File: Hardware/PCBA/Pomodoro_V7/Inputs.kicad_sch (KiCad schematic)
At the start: 2 parts, among them J1 Conn_01x02_Socket

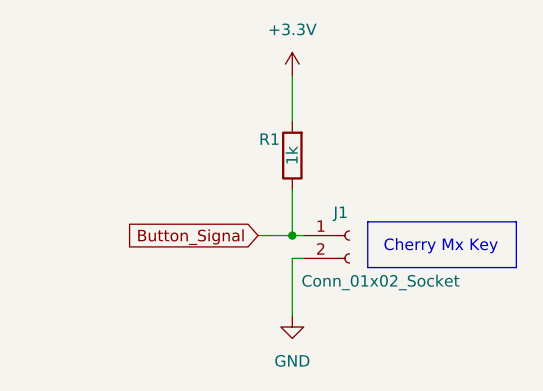
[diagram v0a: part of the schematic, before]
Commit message: Verified the microcontroller Pinout; Added basic peripheral wiring; Added the USBC Wiring
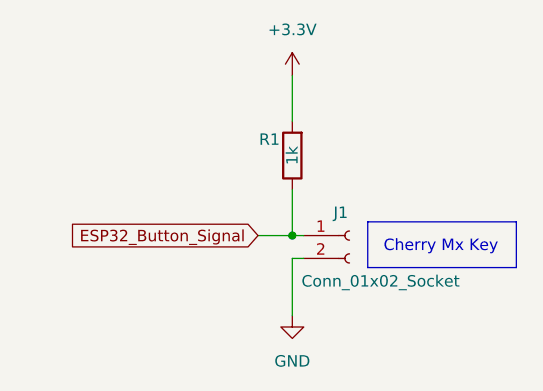
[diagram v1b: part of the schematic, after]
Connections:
- net Button_Signal renamed ESP32_Button_Signal
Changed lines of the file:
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@@
 		)
 	)
-	(global_label "Button_Signal"
+	(global_label "ESP32_Button_Signal"
 		(shape input)
 		(at 49.53 54.61 180)
@@
 		)
 		(property "Intersheetrefs" "${INTERSHEET_REFS}"
-			(at 33.4823 54.61 0)
+			(at 26.4672 54.61 0)
 			(effects
 				(font

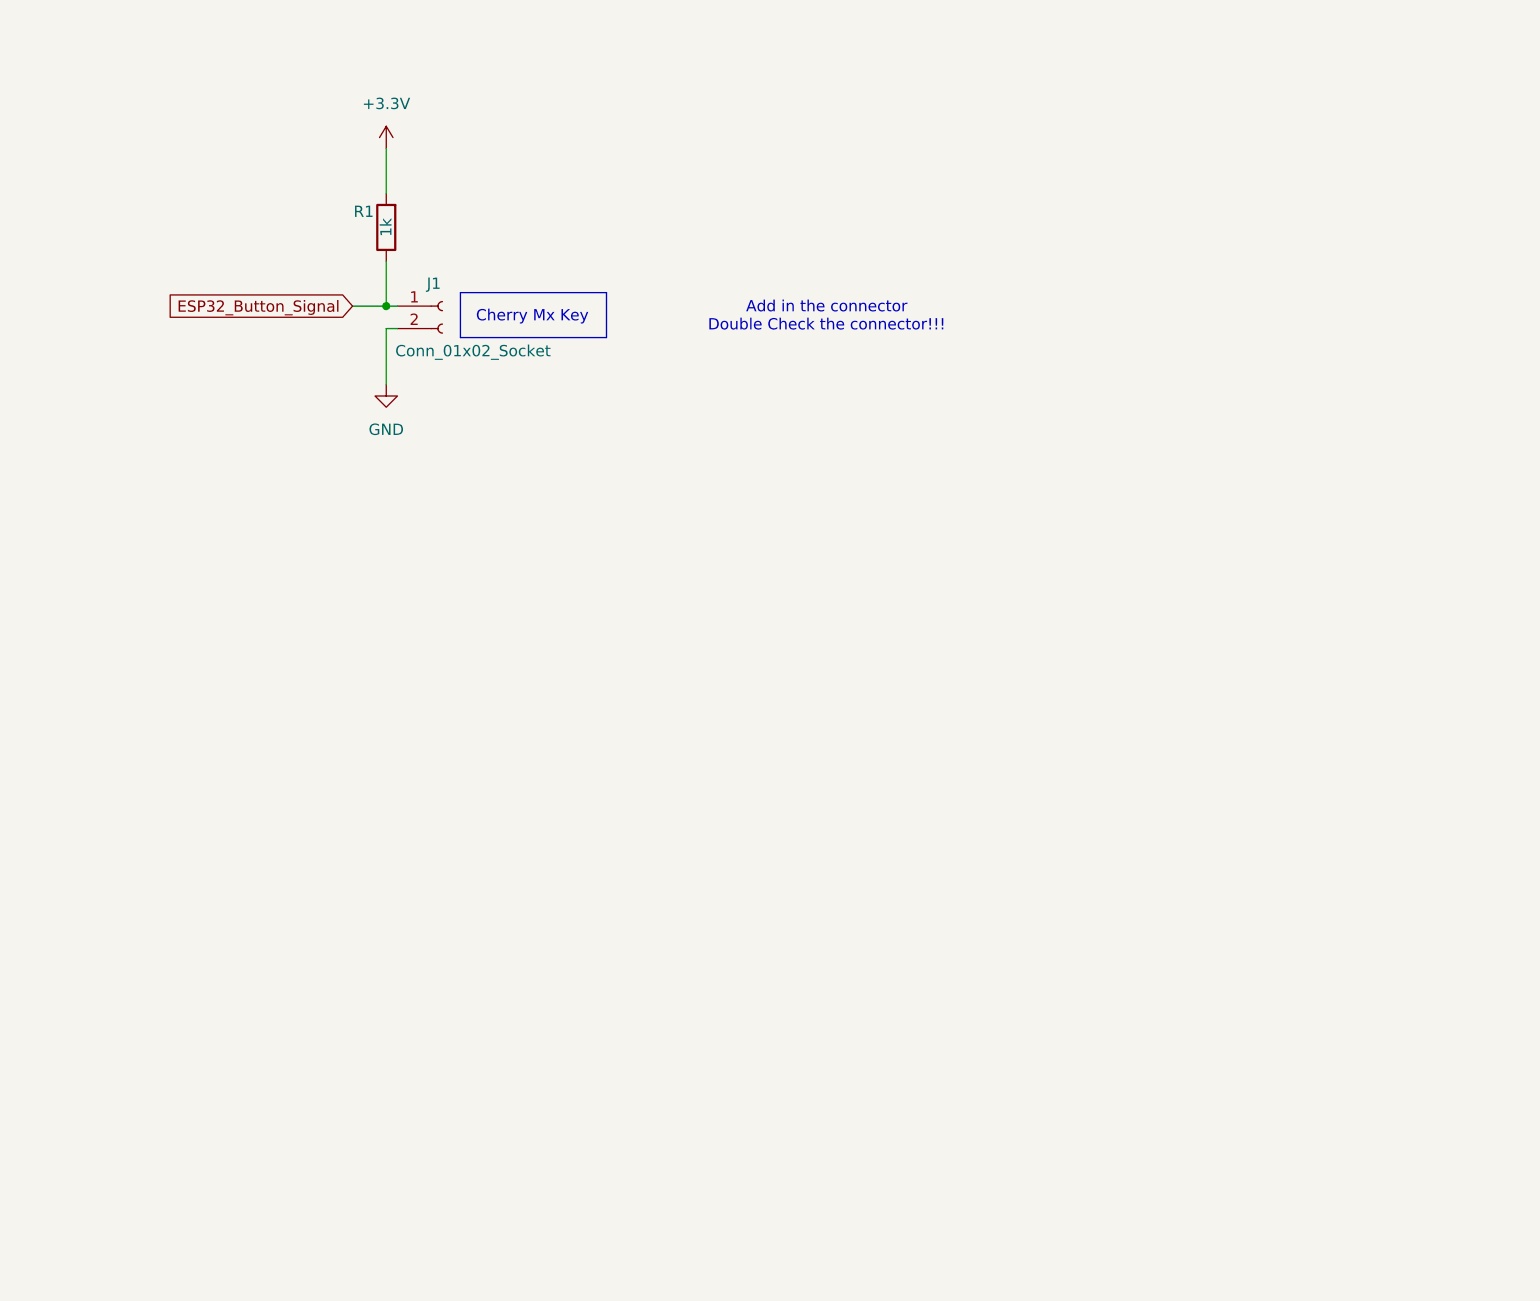
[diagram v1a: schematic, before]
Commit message: FW can now be flashed to an ESP32-S2 Target; Completed the Schematic
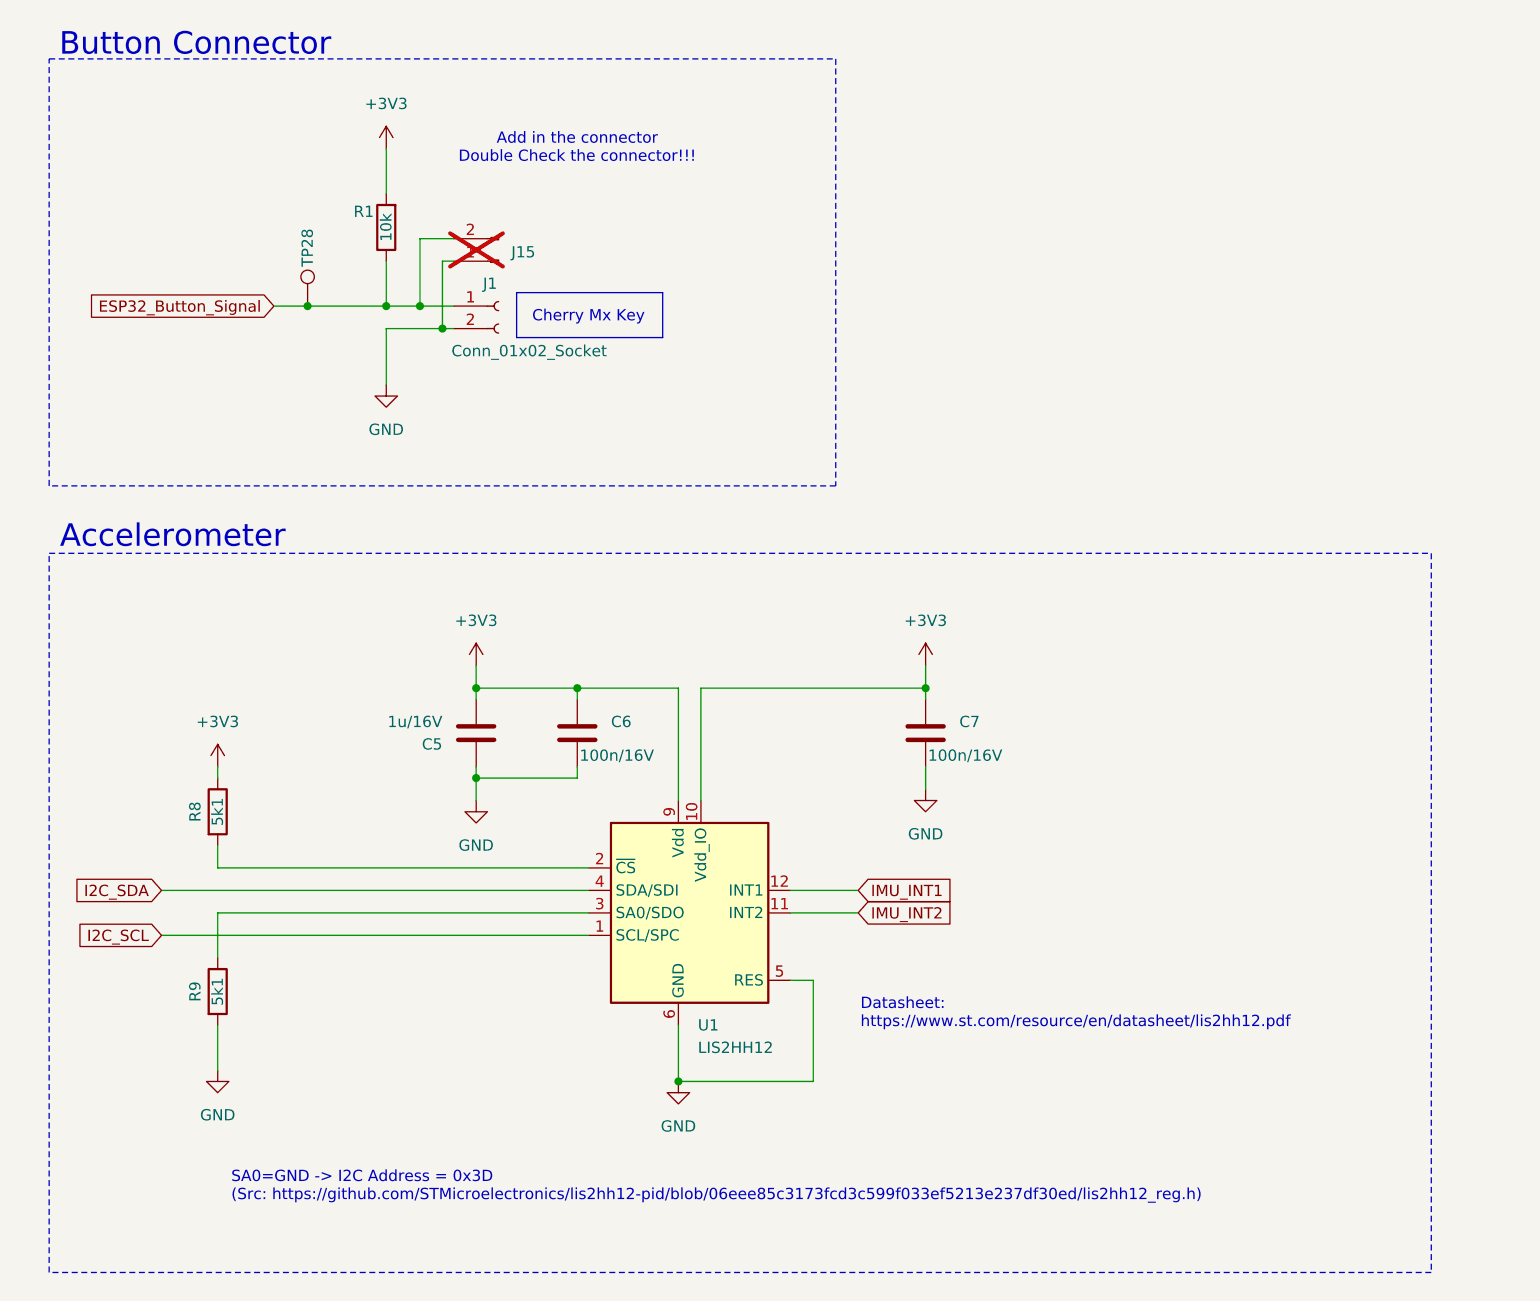
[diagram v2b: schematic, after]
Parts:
- added C5: 1u/16V, Capacitor_SMD:C_0805_2012Metric, symbol Device:C
- added C6, C7: 100n/16V, Capacitor_SMD:C_0805_2012Metric, symbol Device:C
- added J15: Conn_01x02_Pin, Connector_PinHeader_2.54mm:PinHeader_1x02_P2.54mm_Vertical, symbol Connector:Conn_01x02_Pin
- added R8, R9: 5k1, Resistor_SMD:R_0805_2012Metric, symbol Device:R
- added TP28: TestPoint, TestPoint:TestPoint_Pad_D1.0mm, symbol Connector:TestPoint
- added U1: LIS2HH12, Package_LGA:LGA-12_2x2mm_P0.5mm, symbol Sensor_Motion:LIS2HH12
- R1: value 1k -> 10k
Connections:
- net ESP32_Button_Signal: now also J15.2 (Pin_2), TP28.1
- net GND: now also C5.1, C6.1, C7.1, J15.1 (Pin_1), R9.2, U1.5 (RES), U1.6 (GND), U1.7 (GND), U1.8 (GND)
- net +3.3V renamed +3V3
- net +3V3: now also C5.2, C6.2, C7.2, R8.1, U1.10 (Vdd_IO), U1.9 (Vdd)
- new net: R8.2, U1.2 (~{CS})
- new net: R9.1, U1.3 (SA0/SDO)
- new net I2C_SCL: U1.1 (SCL/SPC)
- new net I2C_SDA: U1.4 (SDA/SDI)
- new net IMU_INT1: U1.12 (INT1)
- new net IMU_INT2: U1.11 (INT2)
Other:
- note added: "Accelerometer"
- note added: "Button Connector"
- note added: "Datasheet: https://www.st.com/resource/en/datasheet/lis2hh12.pdf"
- note added: "SA0=GND -> I2C Address = 0x3D (Src: https://github.com/STMicroelectronics/lis2hh12-pid/blob/06eee85c3173fcd3c599f033ef5213e237df30ed/lis2hh12_reg.h)"
- moved on the sheet: J1

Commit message: added the selector wheel, changed the Connectors on the Trigger Button to move the assemlby closer together
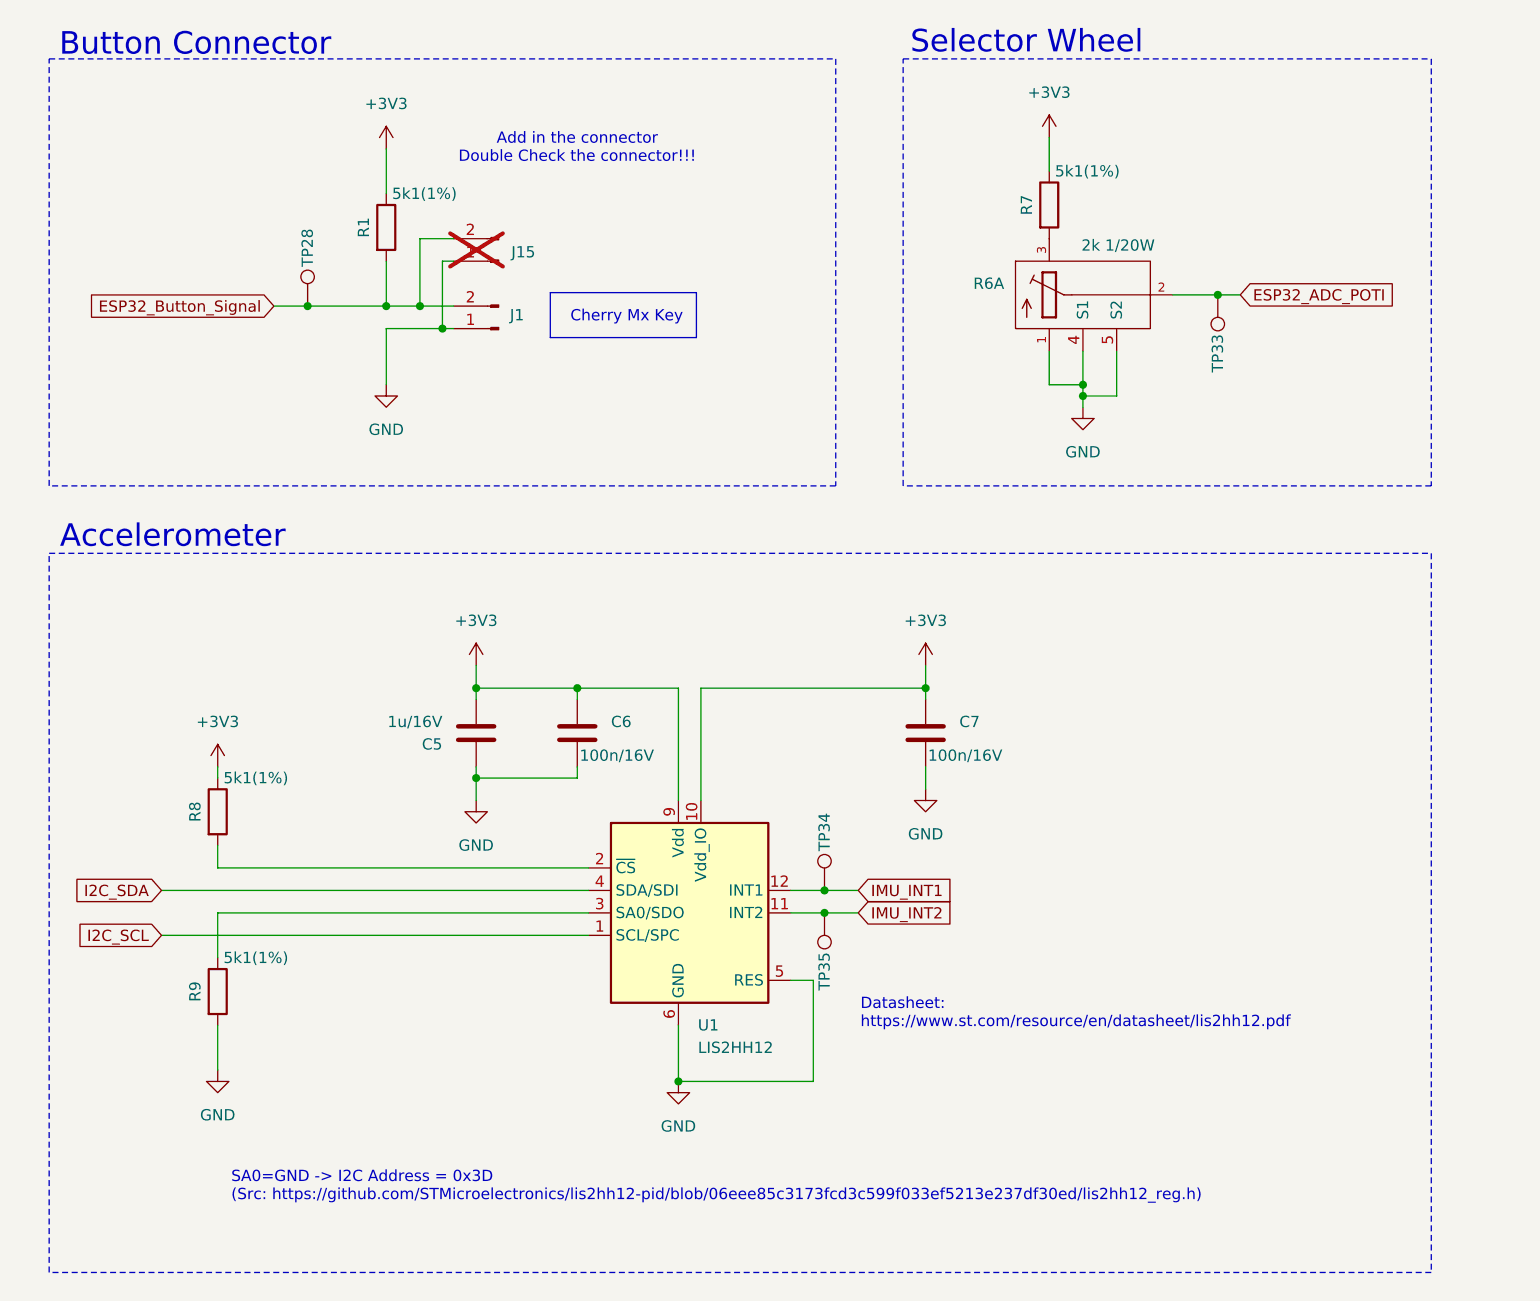
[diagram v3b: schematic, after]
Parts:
- removed J1: Conn_01x02_Socket, Connector_PinSocket_2.54mm:PinSocket_1x02_P2.54mm_Vertical_SMD_Pin1Right, symbol Connector:Conn_01x02_Socket
- added J1: Conn_01x02_Pin, Connector_PinHeader_2.54mm:PinHeader_1x02_P2.54mm_Horizontal, symbol Connector:Conn_01x02_Pin
- added R6: 2k 1/20W, Potentiometer_THT:Pot, symbol PTV09A-4025F-B103:PTV09A-4025F-B103
- added R7: 5k1(1%), Resistor_SMD:R_0805_2012Metric, symbol Device:R
- added TP33, TP34, TP35: TestPoint, TestPoint:TestPoint_Pad_D1.0mm, symbol Connector:TestPoint
- R1: value 10k -> 5k1(1%); MPN RC0805FR-07100RL -> CR0805-FX-5101ELF; Part ID (none) -> CR0805-FX-5101ELF
- R8, R9: value 5k1 -> 5k1(1%)
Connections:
- net +3V3: now also R1.1, R7.1; no longer R1.2
- net ESP32_Button_Signal: now also R1.2, J1.2 (Pin_2); no longer R1.1
- net GND: now also J1.1 (Pin_1), R6.1, R6.4 (S1), R6.5 (S2)
- net IMU_INT1: now also TP34.1
- net IMU_INT2: now also TP35.1
- new net: R6.3, R7.2
- new net ESP32_ADC_POTI: R6.2, TP33.1
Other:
- note added: "Selector Wheel"

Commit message: Update on the PCBA
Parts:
- R6: value 2k 1/20W -> 10k 1/20W; symbol PTV09A-4025F-B103:PTV09A-4025F-B103 -> Device:PTV09A-4025F-B103
- renumbered J1 to J10, J15 to J9, R7 to R4, R1 to R5, R8 to R7, R9 to R8, TP33 to TP22, TP28 to TP23, TP34 to TP24, TP35 to TP25
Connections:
- net GND: now also R6.3; no longer R6.1
- net at R4.2: now also R6.1; no longer R6.3
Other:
- moved on the sheet: R4, TP22

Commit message: Completed the PCBA Design - the formal part
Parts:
- removed J9: Conn_01x02_Pin, Connector_PinHeader_2.54mm:PinHeader_1x02_P2.54mm_Vertical, symbol Connector:Conn_01x02_Pin
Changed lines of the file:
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@@
-	)
-	(junction
-		(at 59.69 57.15)
-		(diameter 0)
-		(color 0 0 0 0)
 	)
 	(junction
@@
 	)
 	(junction
-		(at 57.15 54.61)
-		(diameter 0)
-		(color 0 0 0 0)
-	)
-	(junction
 		(at 63.5 97.79)
 		(diameter 0)
@@
 	(wire
 		(pts
-			(xy 57.15 46.99) (xy 57.15 54.61)
-		)
-		(stroke
-			(width 0)
-			(type default)
-		)
-	)
-	(wire
-		(pts
 			(xy 40.64 54.61) (xy 44.45 54.61)
 		)
@@
 	(wire
 		(pts
-			(xy 53.34 57.15) (xy 59.69 57.15)
+			(xy 53.34 57.15) (xy 60.96 57.15)
 		)
 		(stroke
@@
 	(wire
 		(pts
-			(xy 57.15 54.61) (xy 60.96 54.61)
+			(xy 53.34 54.61) (xy 60.96 54.61)
 		)
 		(stroke
@@
 	(wire
 		(pts
-			(xy 60.96 46.99) (xy 57.15 46.99)
-		)
-		(stroke
-			(width 0)
-			(type default)
-		)
-	)
-	(wire
-		(pts
-			(xy 59.69 49.53) (xy 59.69 57.15)
-		)
-		(stroke
-			(width 0)
-			(type default)
-		)
-	)
-	(wire
-		(pts
 			(xy 86.36 135.89) (xy 86.36 142.24)
 		)
@@
 	(wire
 		(pts
-			(xy 53.34 54.61) (xy 57.15 54.61)
-		)
-		(stroke
-			(width 0)
-			(type default)
-		)
-	)
-	(wire
-		(pts
 			(xy 146.05 33.02) (xy 146.05 35.56)
 		)
@@
 	(wire
 		(pts
-			(xy 60.96 49.53) (xy 59.69 49.53)
-		)
-		(stroke
-			(width 0)
-			(type default)
-		)
-	)
-	(wire
-		(pts
 			(xy 63.5 97.79) (xy 74.93 97.79)
 		)
@@
 		(pts
 			(xy 53.34 63.5) (xy 53.34 57.15)
-		)
-		(stroke
-			(width 0)
-			(type default)
-		)
-	)
-	(wire
-		(pts
-			(xy 59.69 57.15) (xy 60.96 57.15)
 		)
 		(stroke
@@
 	)
 	(symbol
-		(lib_id "Connector:Conn_01x02_Pin")
-		(at 66.04 49.53 180)
-		(unit 1)
-		(exclude_from_sim no)
-		(in_bom no)
-		(on_board yes)
-		(dnp yes)
-		(property "Reference" "J9"
-			(at 68.834 48.514 0)
-			(effects
-				(font
-					(size 1.27 1.27)
-				)
-			)
-		)
-		(property "Value" "Conn_01x02_Pin"
-			(at 65.405 52.07 0)
-			(effects
-				(font
-					(size 1.27 1.27)
-				)
-				(hide yes)
-			)
-		)
-		(property "Footprint" "Connector_PinHeader_2.54mm:PinHeader_1x02_P2.54mm_Vertical"
-			(at 66.04 49.53 0)
-			(effects
-				(font
-					(size 1.27 1.27)
-				)
-				(hide yes)
-			)
-		)
-		(property "Datasheet" "~"
-			(at 66.04 49.53 0)
-			(effects
-				(font
-					(size 1.27 1.27)
-				)
-				(hide yes)
-			)
-		)
-		(property "Description" "Generic connector, single row, 01x02, script generated"
-			(at 66.04 49.53 0)
-			(effects
-				(font
-					(size 1.27 1.27)
-				)
-				(hide yes)
-			)
-		)
-		(pin "2"
-		)
-		(pin "1"
-		)
-		(instances
-			(project "Pomodoro_V7"
-				(path "/7b50fc13-bee1-48b7-8eab-d6ef36855383/c8f67831-bbf6-4683-a2c8-3e9cad0fb84c"
-					(reference "J9")
-					(unit 1)
-				)
-			)
-		)
-	)
-	(symbol
 		(lib_id "Device:PTV09A-4025F-B103")
 		(at 146.05 50.8 0)
@@
 			)
 		)
-		(property "Datasheet" ""
+		(property "Datasheet" "https://eu.mouser.com/datasheet/2/54/ptv09-777818.pdf"
 			(at 146.05 50.8 0)
 			(effects
@@
 		(lib_id "Device:R")
 		(at 34.29 132.08 0)
+		(mirror y)
 		(unit 1)
 		(exclude_from_sim no)
@@
 		(dnp no)
 		(property "Reference" "R8"
-			(at 31.75 132.08 90)
+			(at 36.83 132.08 90)
 			(effects
 				(font
@@
 		)
 		(property "Value" "5k1(1%)"
-			(at 38.608 128.27 0)
+			(at 29.972 128.27 0)
 			(effects
 				(font
@@
 		)
 		(property "Footprint" "Resistor_SMD:R_0805_2012Metric"
-			(at 32.512 132.08 90)
-			(effects
-				(font
+			(at 36.068 132.08 90)
+			(effects
+				(font

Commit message: Updated the PCBA Files
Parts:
- C5: value 1u/16V -> 1u/16V+/X5R
- C6, C7: value 100n/16V -> 100n/16V+/X5R
- J10: Notes (none) -> Horizontal generic Pin Header
- R6: Mfg Part # (none) -> PTV09A-4025F-B103
- TP22, TP23, TP24, TP25: now not fitted
- U1: footprint Package_LGA:LGA-12_2x2mm_P0.5mm -> Package_LGA:Kionix_LGA-12_2x2mm_P0.5mm_LayoutBorder2x4y; Mfg Part # (none) -> LIS2HH12TR
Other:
- note removed: "Add in the connector Double Check the connector!!!"
- note removed: "Cherry Mx Key"
- moved on the sheet: C5, C6, R4, R5, R6, R7, R8, U1
